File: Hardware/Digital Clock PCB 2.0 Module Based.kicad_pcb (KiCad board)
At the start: 2 copper layers, 124.5 x 46 mm, 77 parts, among them J1 USB_C_Receptacle_USB2.0, J2 Conn_01x04, J3 Conn_01x04, Q1 C15127, Q2 C8545, SW1 SW_Push, SW2 SW_Push, U1 ESP32-S2-SOLO-2, U10 SBC18-11SURKCGKWA, U2 AMS1117-3.3, U3 74LS47, U4 74LS47, U5 SBC18-11SURKCGKWA, U6 SBC18-11SURKCGKWA, U7 74LS47, U8 74LS47, U9 SBC18-11SURKCGKWA

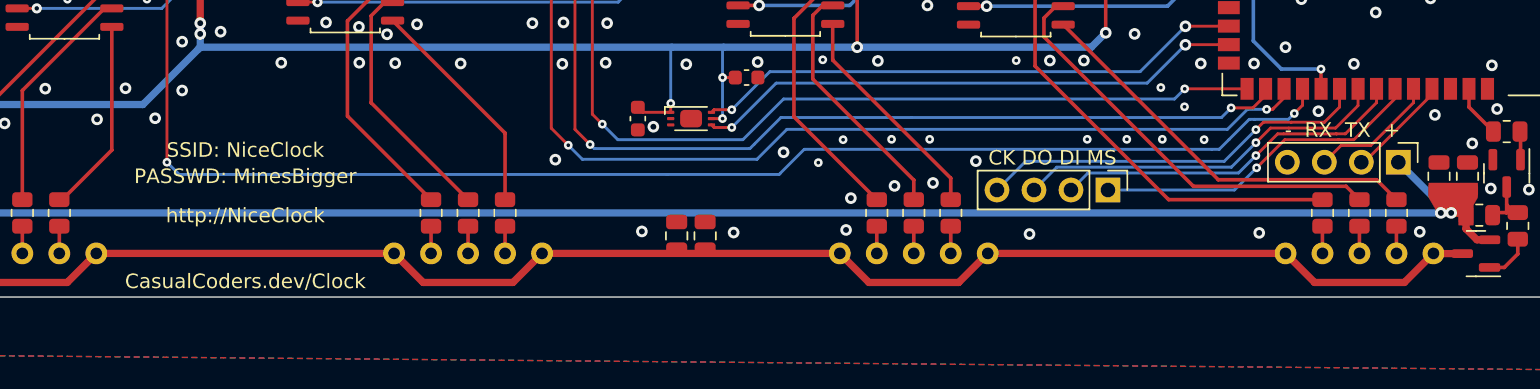
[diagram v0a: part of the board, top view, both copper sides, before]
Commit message: Move firmware down a directory. Add Integration test. Requires gitignored file containing wifi credentials.
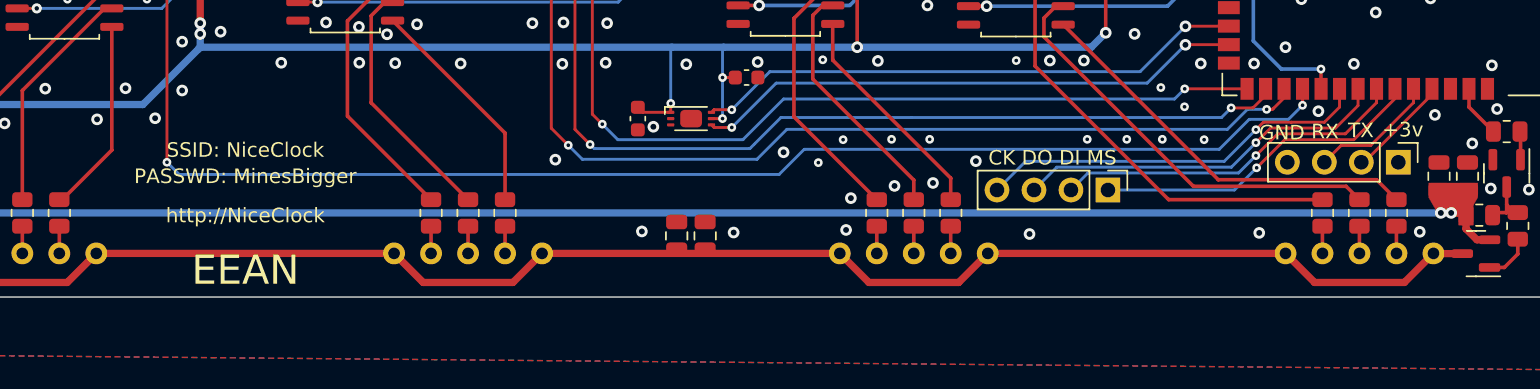
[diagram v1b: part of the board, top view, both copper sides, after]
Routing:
- net VBUS: track 149.3 -> 143.4 mm
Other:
- board text added: "+3v"
- board text added: "EEAN"
- board text added: "GND"
- board text added: "RX"
- board text added: "TX"
- board text removed: "- RX TX +"
- board text removed: "CasualCoders.dev/Clock"
